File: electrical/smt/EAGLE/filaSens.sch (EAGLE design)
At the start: 16 parts, among them IC2 SS495, IC3 TINY85

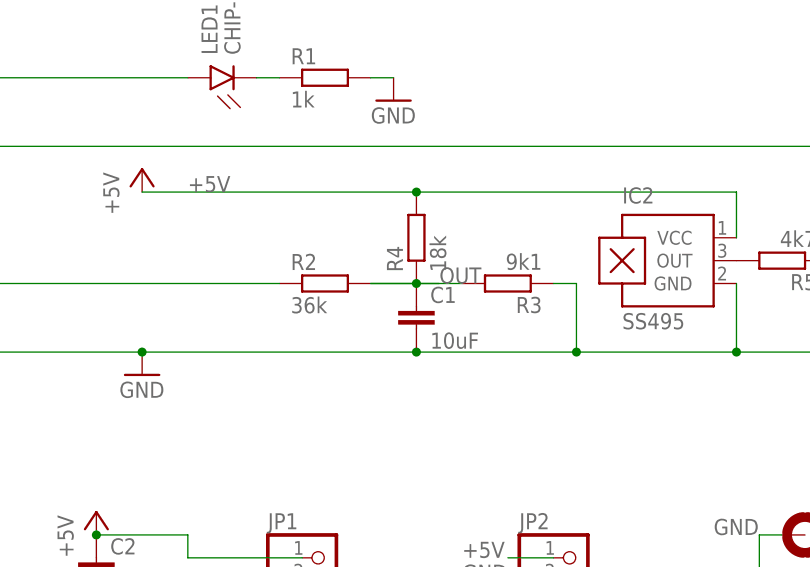
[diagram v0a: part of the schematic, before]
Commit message: change EAGLE files to capture PR #28 and Issue #27
change EAGLE files to capture PR #28 and Issue #27

Update GERBER files as well as EAGLE files
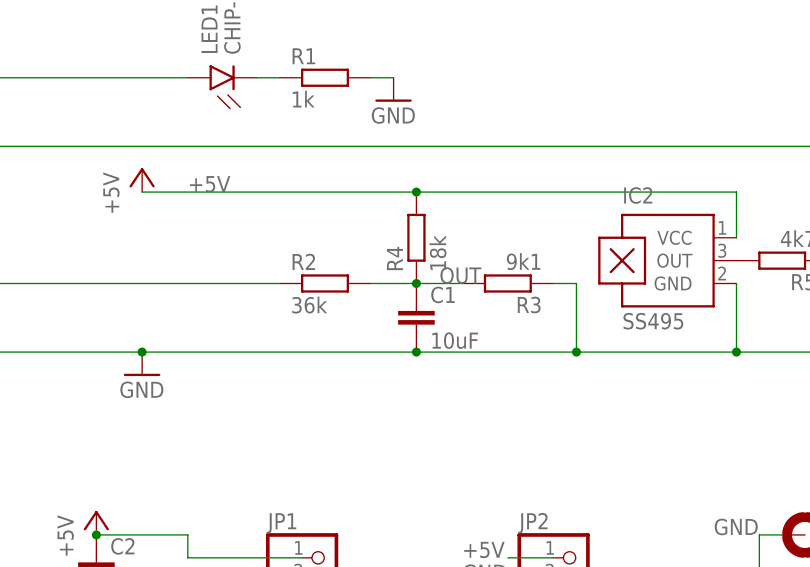
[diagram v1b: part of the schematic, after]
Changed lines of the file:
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@@
 <drawing>
 <settings>
-<setting alwaysvectorfont="no"/>
+<setting alwaysvectorfont="yes"/>
 <setting keepoldvectorfont="yes"/>
 <setting verticaltext="up"/>
@@
 <net name="OUT" class="0">
 <segment>
-<wire x1="96.52" y1="48.26" x2="88.9" y2="48.26" width="0.1524" layer="91"/>
 <wire x1="99.06" y1="48.26" x2="93.98" y2="48.26" width="0.1524" layer="91"/>
 <label x="96.52" y="48.26" size="1.778" layer="95"/>

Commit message: Fixed cap gnd, made 5v trace larger, re-routed some traces to be cleaner
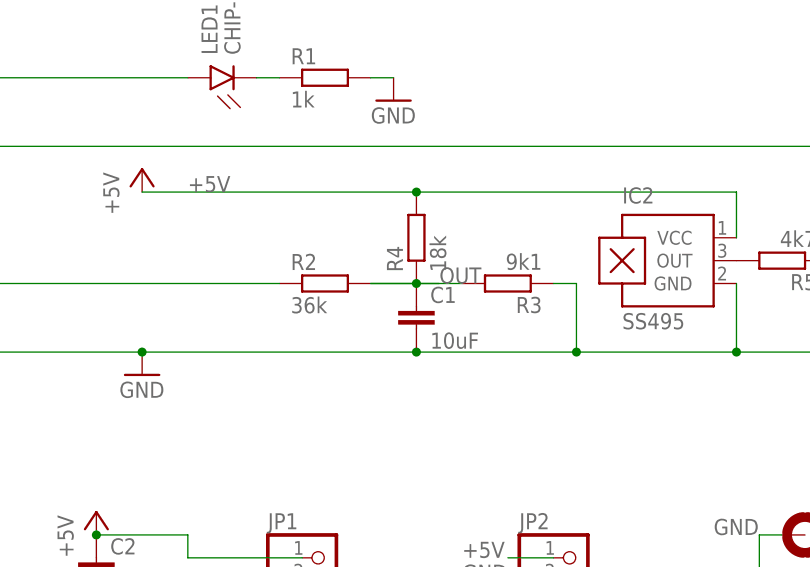
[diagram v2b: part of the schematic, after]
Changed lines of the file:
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@@
 <drawing>
 <settings>
-<setting alwaysvectorfont="yes"/>
+<setting alwaysvectorfont="no"/>
 <setting keepoldvectorfont="yes"/>
 <setting verticaltext="up"/>
@@
 <net name="OUT" class="0">
 <segment>
+<wire x1="96.52" y1="48.26" x2="88.9" y2="48.26" width="0.1524" layer="91"/>
 <wire x1="99.06" y1="48.26" x2="93.98" y2="48.26" width="0.1524" layer="91"/>
 <label x="96.52" y="48.26" size="1.778" layer="95"/>
